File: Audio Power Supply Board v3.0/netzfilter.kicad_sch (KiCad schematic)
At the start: 0 parts

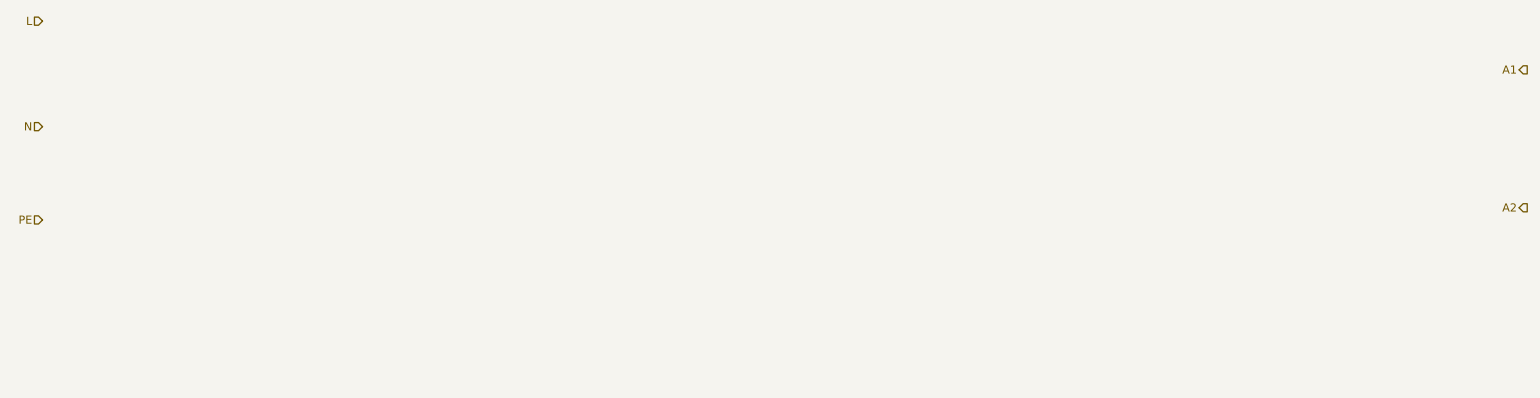
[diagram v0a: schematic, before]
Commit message: Change to a modular drawing and design
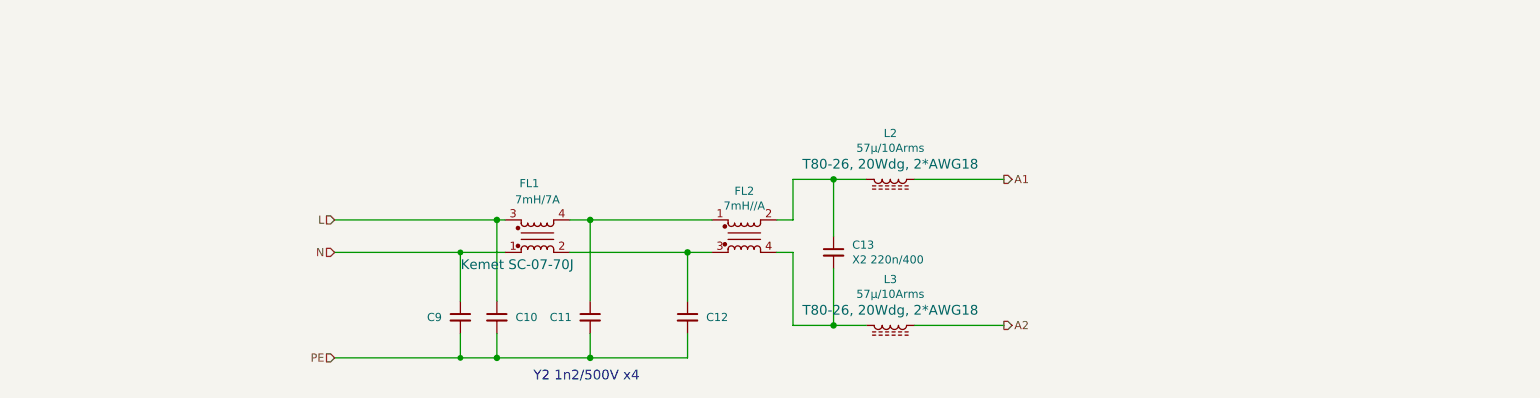
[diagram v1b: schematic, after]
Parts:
- added C10, C11, C12, C9: Y2 1n2/500, Capacitor_THT:C_Rect_L18.0mm_W7.0mm_P15.00mm_FKS3_FKP3, symbol Device:C_Small
- added C13: X2 220n/400, Capacitor_THT:C_Rect_L18.0mm_W8.0mm_P15.00mm_FKS3_FKP3, symbol Device:C_Small
- added FL1: 7mH/7A, Userlibrary:L_CommonMode_Toroid_Vertical_L35mm_W25mm_Px19mm_Py18mm_Kemet_SC07_70J, symbol Device:Filter_EMI_LL
- added FL2: 7mH//A, Userlibrary:L_CommonMode_Toroid_Vertical_L35mm_W25mm_Px19mm_Py18mm_Kemet_SC07_70J, symbol Device:Filter_EMI_LL
- added L2, L3: 57µ/10Arms, Userlibrary:L_muRata_6000A, symbol Device:L_Ferrite
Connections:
- net A1: now also L2.1
- net A2: now also L3.1
- net L: now also C10.1, FL1.3
- net N: now also C9.1, FL1.1
- net PE: now also C10.2, C11.2, C12.2, C9.2
- new net: C12.1, FL1.2, FL2.3
- new net: C11.1, FL1.4, FL2.1
- new net: C13.1, FL2.2, L2.2
- new net: C13.2, FL2.4, L3.2
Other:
- note added: "Y2 1n2/500V x4"
